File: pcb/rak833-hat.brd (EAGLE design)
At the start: 65 x 56 mm, 8 parts, among them IC2 AMS1117-3.3, K1 PIN20X2

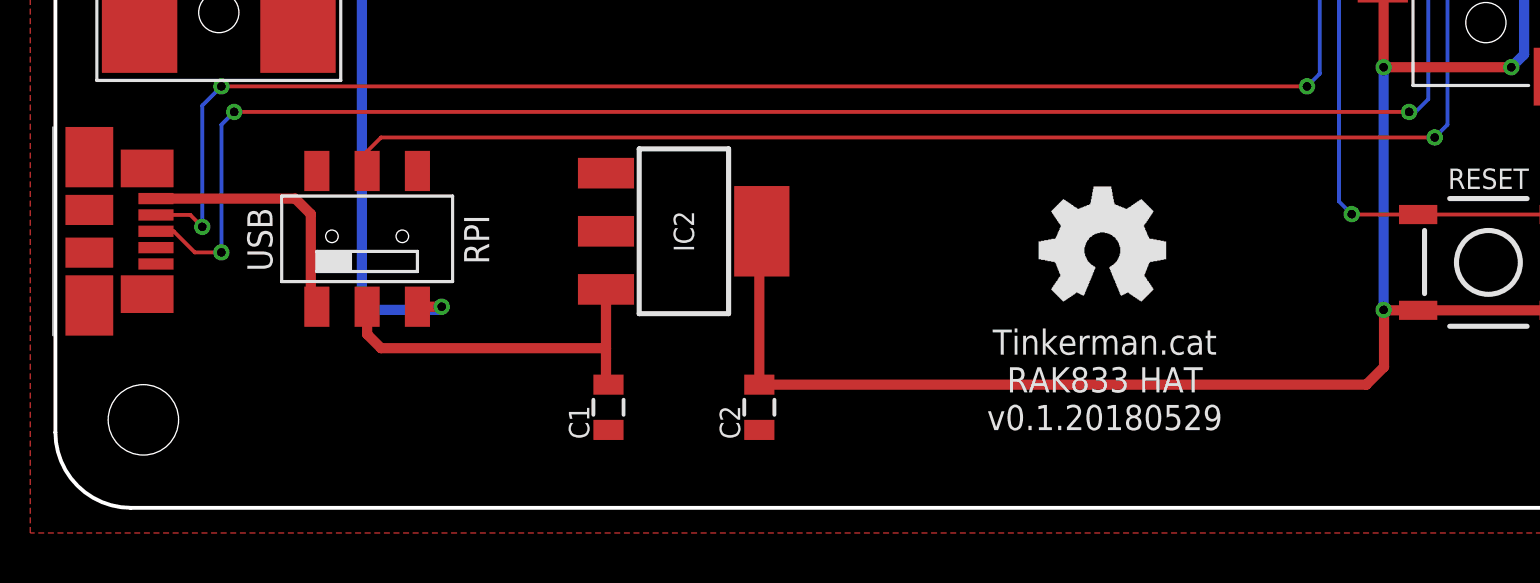
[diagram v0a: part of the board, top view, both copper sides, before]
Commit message: Fixing switch footprint
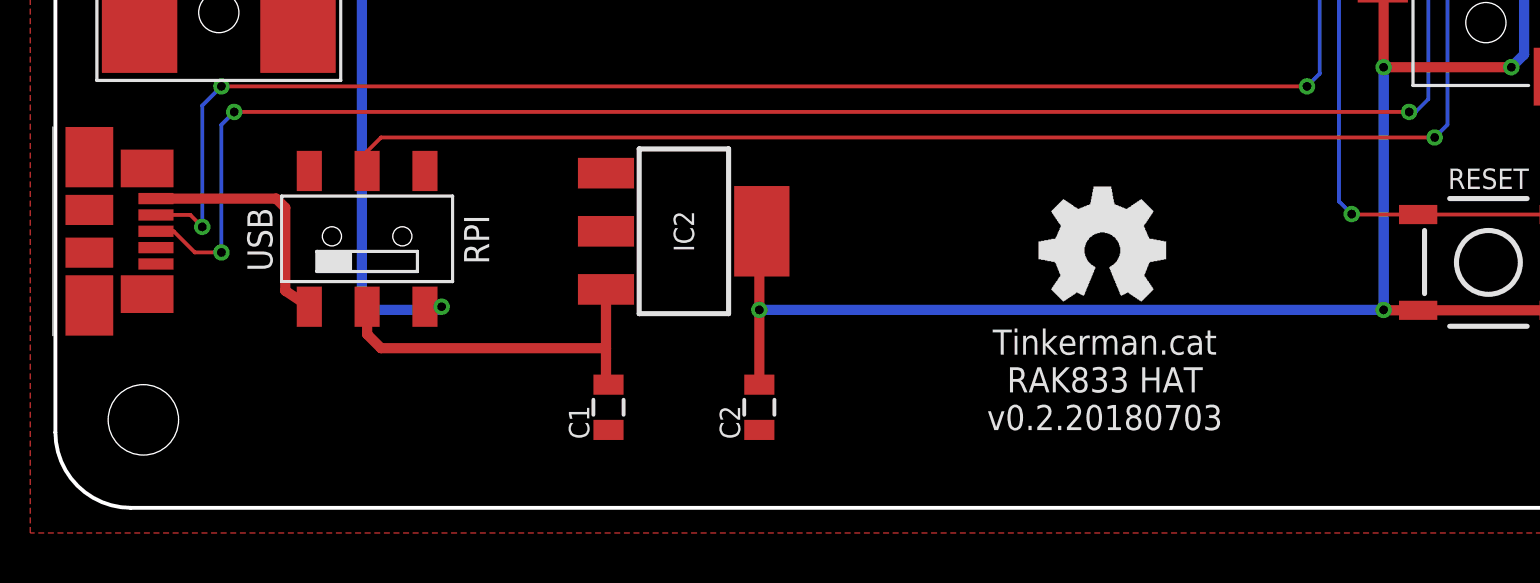
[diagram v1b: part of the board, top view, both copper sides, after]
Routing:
- net 3V3: track 98.7 -> 96.2 mm, vias 6 -> 7
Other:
- board text added: "Tinkerman.cat RAK833 HAT v0.2.20180703"
- board text removed: "Tinkerman.cat RAK833 HAT v0.1.20180529"
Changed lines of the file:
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@@
 <text x="41.742" y="5.092" size="1" layer="25" font="vector" ratio="16" rot="R180" align="center">Tinkerman.cat
 RAK833 HAT
-v0.1.20180529</text>
+v0.2.20180703</text>
 <rectangle x1="43.1692" y1="8.2103" x2="43.22" y2="8.2357" layer="25" rot="R180"/>
 <rectangle x1="40.0704" y1="8.2103" x2="40.1212" y2="8.2357" layer="25" rot="R180"/>
@@
 <contactref element="U$1" pad="C1"/>
 <wire x1="8.37" y1="53.77" x2="10.91" y2="53.77" width="0.4064" layer="16"/>
-<wire x1="14.4" y1="8" x2="15.366" y2="8" width="0.4064" layer="1"/>
+<wire x1="14.7" y1="8" x2="15.366" y2="8" width="0.4064" layer="1"/>
 <wire x1="12.192" y1="53.25" x2="12.192" y2="8.382" width="0.4064" layer="16"/>
 <via x="15.366" y="8" extent="1-16" drill="0.35"/>
@@
 <contactref element="RESET" pad="3"/>
 <contactref element="C2" pad="2"/>
-<wire x1="28" y1="4.9" x2="28" y2="10.901" width="0.4064" layer="1"/>
+<wire x1="28" y1="4.9" x2="28" y2="7.874" width="0.4064" layer="1"/>
+<wire x1="28" y1="7.874" x2="28" y2="10.901" width="0.4064" layer="1"/>
 <wire x1="28" y1="10.901" x2="28.099" y2="11" width="0.3048" layer="1"/>
 <wire x1="54.206" y1="7.857" x2="54.356" y2="7.857" width="0.3048" layer="1"/>
@@
 <wire x1="52.832" y1="7.874" x2="52.849" y2="7.857" width="0.4064" layer="1"/>
 <wire x1="52.849" y1="7.857" x2="54.206" y2="7.857" width="0.4064" layer="1"/>
-<wire x1="52.849" y1="5.605" x2="52.849" y2="7.857" width="0.4064" layer="1"/>
-<wire x1="28" y1="4.9" x2="52.144" y2="4.9" width="0.4064" layer="1"/>
-<wire x1="52.144" y1="4.9" x2="52.849" y2="5.605" width="0.4064" layer="1"/>
 <wire x1="58.42" y1="18.034" x2="57.912" y2="17.526" width="0.4064" layer="16"/>
 <via x="57.912" y="17.526" extent="1-16" drill="0.35"/>
 <wire x1="57.912" y1="17.526" x2="52.832" y2="17.526" width="0.4064" layer="1"/>
+<wire x1="52.832" y1="7.874" x2="28" y2="7.874" width="0.4064" layer="16"/>
+<wire x1="27.94" y1="7.874" x2="28" y2="7.874" width="0.4064" layer="16"/>
+<via x="28" y="7.874" extent="1-16" drill="0.35"/>
 </signal>
 <signal name="PCIE_SCK">
@@
 <signal name="USB_5V">
 <contactref element="U$1" pad="B1"/>
-<wire x1="10.16" y1="11.684" x2="10.16" y2="8.24" width="0.4064" layer="1"/>
-<wire x1="10.16" y1="8.24" x2="10.4" y2="8" width="0.3048" layer="1"/>
+<wire x1="10.16" y1="8.24" x2="10.1" y2="8" width="0.3048" layer="1"/>
 <contactref element="U$2" pad="VCC"/>
-<wire x1="4" y1="12.3" x2="9.544" y2="12.3" width="0.4064" layer="1"/>
-<wire x1="9.544" y1="12.3" x2="10.16" y2="11.684" width="0.4064" layer="1"/>
+<wire x1="4" y1="12.3" x2="8.782" y2="12.3" width="0.4064" layer="1"/>
+<wire x1="8.782" y1="12.3" x2="9.144" y2="11.938" width="0.4064" layer="1"/>
+<wire x1="9.144" y1="11.938" x2="9.144" y2="8.636" width="0.4064" layer="1"/>
+<wire x1="9.144" y1="8.636" x2="10.1" y2="8" width="0.4064" layer="1"/>
 </signal>
 </signals>
